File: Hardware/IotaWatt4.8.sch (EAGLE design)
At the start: 53 parts

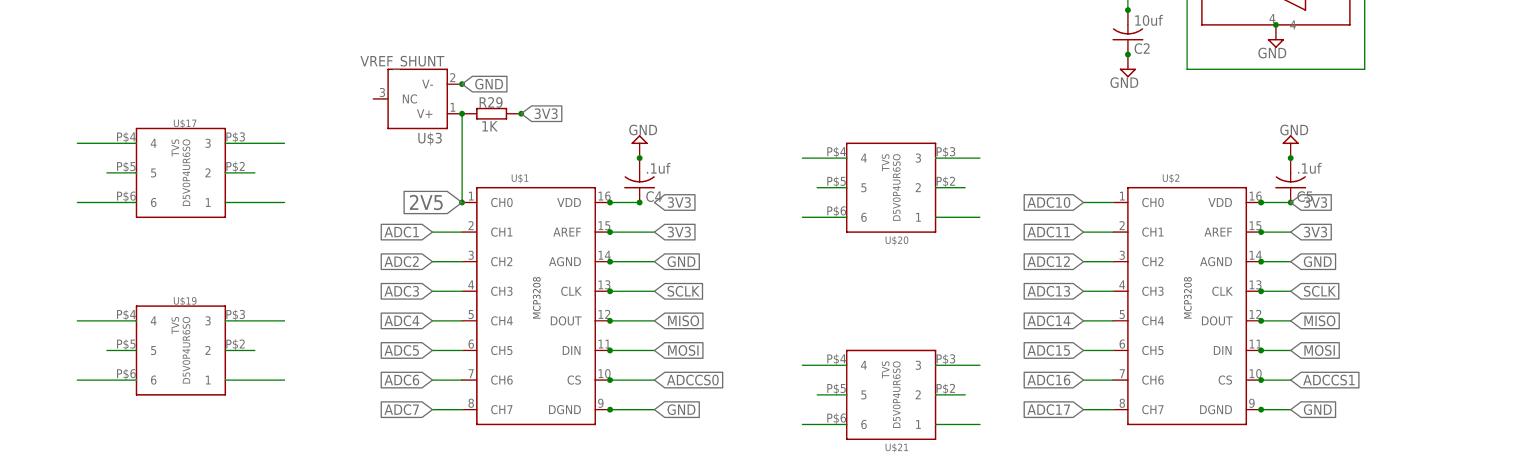
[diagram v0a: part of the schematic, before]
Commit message: corrected a major mistake
I had connected MOSI/MISO/SCLK to the primary hw SPI - now they are correctly conntected to the secondary bus.
MOSI->HSPI-D(GPIO13)
MISO->HSPI-Q(GPIO12)
SCLK->HSPI-CLK(GPIO14)
CSSD->HSPI-CD(GPIO15)

also added some minor changes to better fit the case
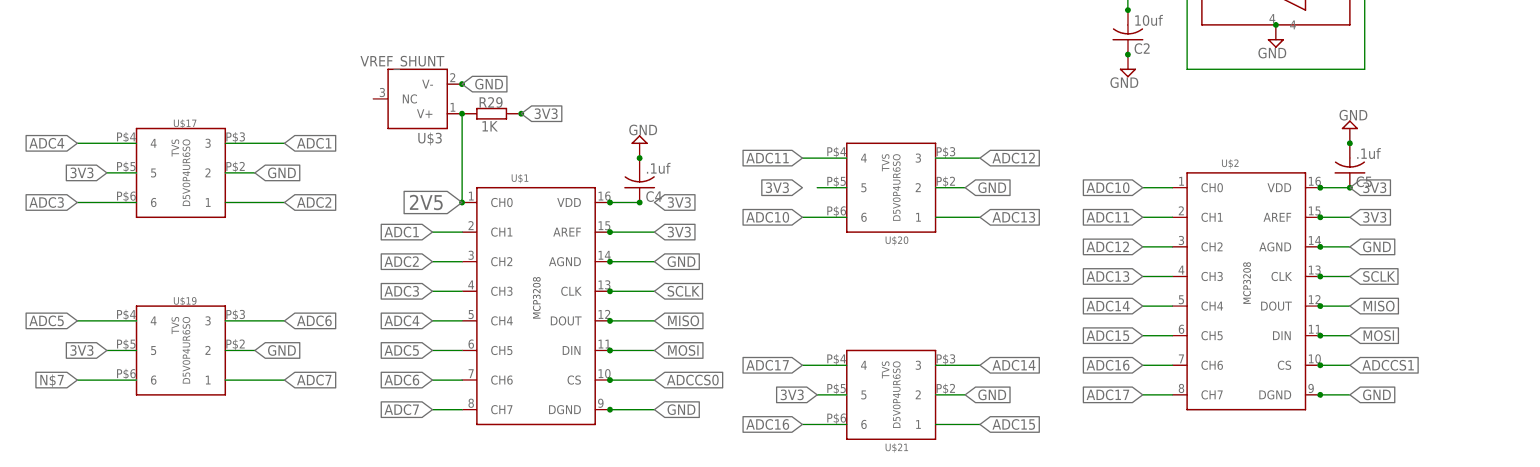
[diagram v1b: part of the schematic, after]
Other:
- moved on the sheet: C5, U$2

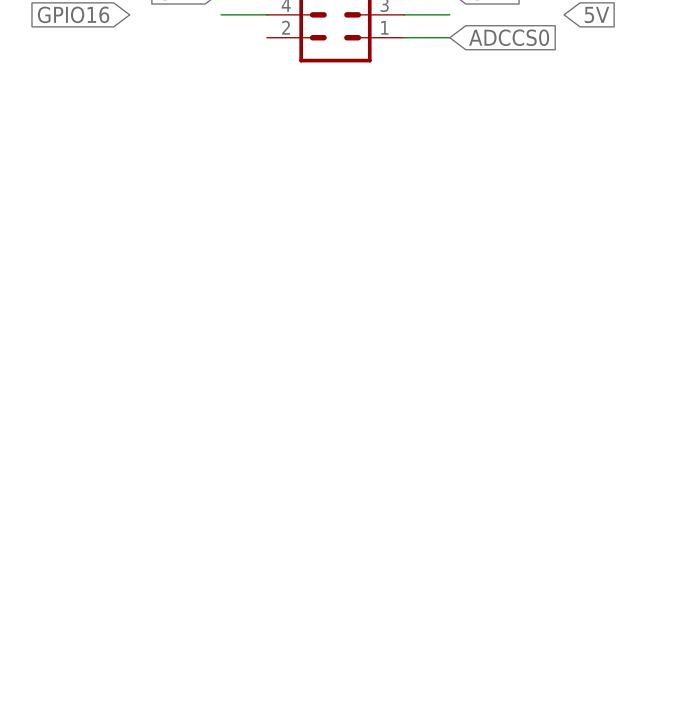
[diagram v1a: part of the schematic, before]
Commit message: SPI termination resistor positions
added SPI termination resistor positions
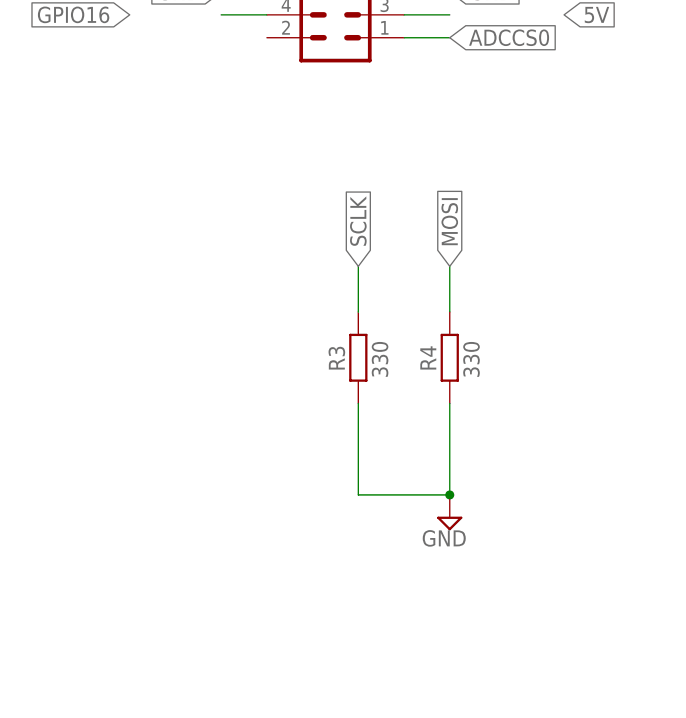
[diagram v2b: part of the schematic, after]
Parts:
- added R3, R4: 330, resistor:R-EU_R0805
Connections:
- net GND: now also R3.1, R4.1
- net MOSI: now also R4.2
- net SCLK: now also R3.2
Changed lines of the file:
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@@
 <part name="C9" library="adafruit" deviceset="C-US" device="C0805" value="10uF"/>
 <part name="R32" library="resistor" deviceset="R-EU_" device="R0805" value="12K"/>
+<part name="R3" library="resistor" deviceset="R-EU_" device="R0805" value="330"/>
+<part name="R4" library="resistor" deviceset="R-EU_" device="R0805" value="330"/>
+<part name="SUPPLY2" library="supply2" deviceset="GND" device=""/>
 </parts>
 <sheets>
@@
 <instance part="C9" gate="G$1" x="73.66" y="99.06" rot="MR270"/>
 <instance part="R32" gate="G$1" x="83.82" y="99.06" rot="MR0"/>
+<instance part="R3" gate="G$1" x="238.76" y="-22.86" smashed="yes" rot="R90">
+<attribute name="NAME" x="237.2614" y="-24.384" size="1.778" layer="95" rot="R90"/>
+<attribute name="VALUE" x="242.062" y="-25.146" size="1.778" layer="96" rot="R90"/>
+</instance>
+<instance part="R4" gate="G$1" x="248.92" y="-22.86" smashed="yes" rot="R90">
+<attribute name="NAME" x="247.4214" y="-24.384" size="1.778" layer="95" rot="R90"/>
+<attribute name="VALUE" x="252.222" y="-25.146" size="1.778" layer="96" rot="R90"/>
+</instance>
+<instance part="SUPPLY2" gate="GND" x="248.92" y="-40.64" rot="MR0"/>
 </instances>
 <busses>
@@
 <wire x1="228.6" y1="25.4" x2="223.52" y2="25.4" width="0.1524" layer="91"/>
 <label x="213.36" y="25.4" size="1.778" layer="91" font="vector" rot="R180" xref="yes"/>
+</segment>
+<segment>
+<pinref part="R3" gate="G$1" pin="1"/>
+<wire x1="238.76" y1="-27.94" x2="238.76" y2="-38.1" width="0.1524" layer="91"/>
+<pinref part="R4" gate="G$1" pin="1"/>
+<wire x1="238.76" y1="-38.1" x2="248.92" y2="-38.1" width="0.1524" layer="91"/>
+<wire x1="248.92" y1="-38.1" x2="248.92" y2="-27.94" width="0.1524" layer="91"/>
+<pinref part="SUPPLY2" gate="GND" pin="GND"/>
+<junction x="248.92" y="-38.1"/>
 </segment>
 </net>
@@
 <label x="261.62" y="20.32" size="1.778" layer="91" font="vector" xref="yes"/>
 </segment>
+<segment>
+<pinref part="R4" gate="G$1" pin="2"/>
+<wire x1="248.92" y1="-17.78" x2="248.92" y2="-12.7" width="0.1524" layer="91"/>
+<label x="248.92" y="-12.7" size="1.778" layer="95" rot="R90" xref="yes"/>
+</segment>
 </net>
 <net name="SCLK" class="0">
@@
 <label x="248.92" y="22.86" size="1.778" layer="91" font="vector" xref="yes"/>
 </segment>
-</net>
+<segment>
+<pinref part="R3" gate="G$1" pin="2"/>
+<wire x1="238.76" y1="-17.78" x2="238.76" y2="-12.7" width="0.1524" layer="91"/>
+<label x="238.76" y="-12.7" size="1.778" layer="95" rot="R90" xref="yes"/>
+</segment>
+</net>

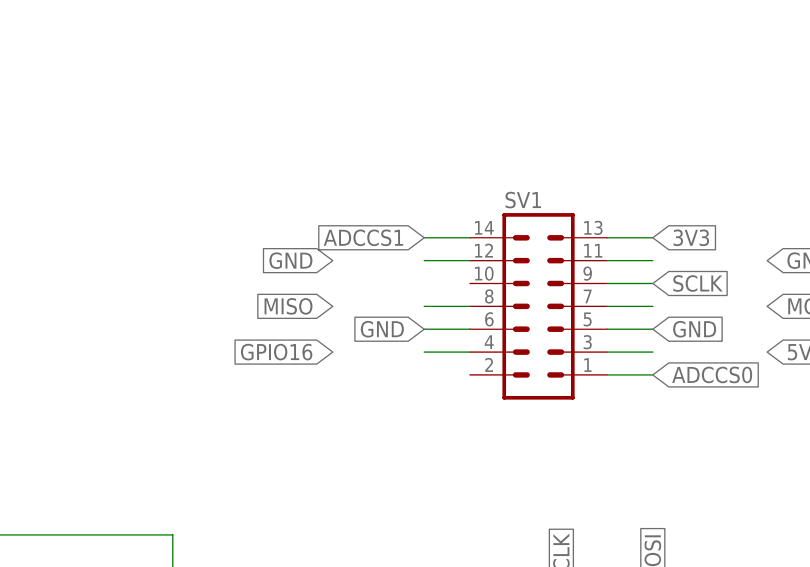
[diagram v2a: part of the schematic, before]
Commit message: mechanical fitting
moved the clamp positions such that they should fit unmodified.
Added silkscreen signal names for the power board ribbon connector, improved 3V3 connection on IO Board
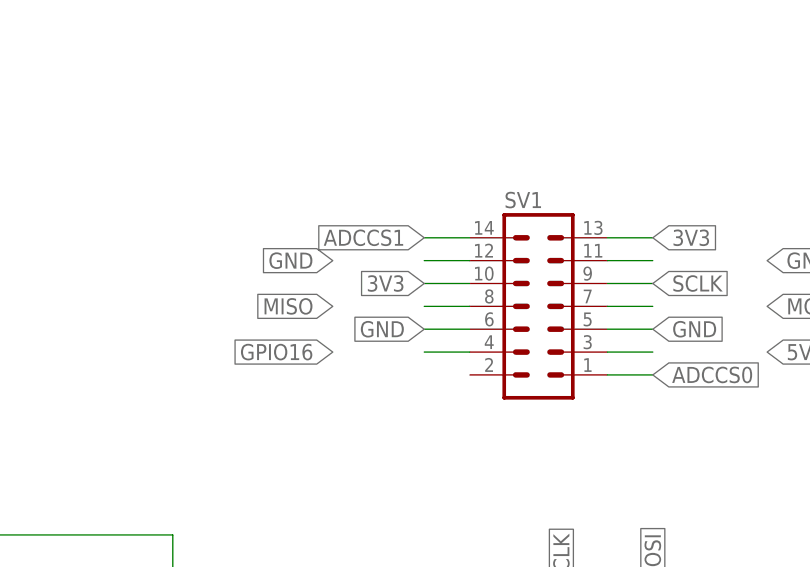
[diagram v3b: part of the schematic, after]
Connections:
- net 3V3: now also SV1.10
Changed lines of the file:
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@@
 <label x="248.92" y="27.94" size="1.778" layer="91" font="vector" xref="yes"/>
+</segment>
+<segment>
+<pinref part="SV1" gate="G$1" pin="10"/>
+<wire x1="228.6" y1="22.86" x2="223.52" y2="22.86" width="0.1524" layer="91"/>
+<label x="223.52" y="22.86" size="1.778" layer="95" rot="R180" xref="yes"/>
 </segment>
 </net>
